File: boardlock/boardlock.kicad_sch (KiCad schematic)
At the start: 3 parts, among them U6 ESP32-S3-WROOM-1

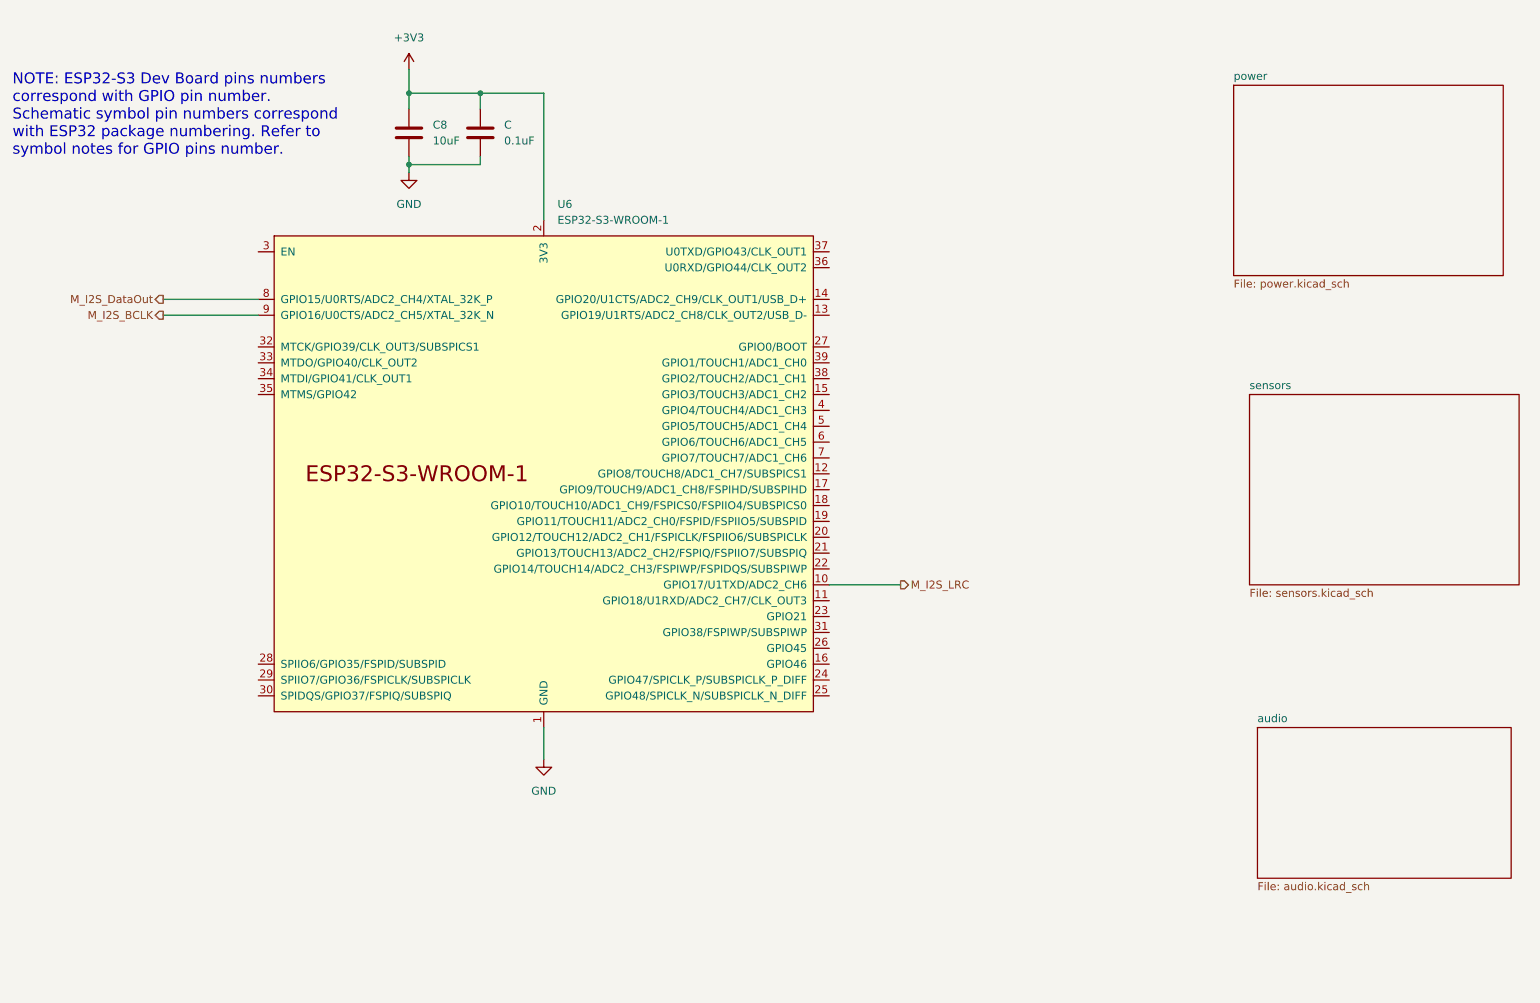
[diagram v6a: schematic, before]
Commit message: Added power library and fixed labels
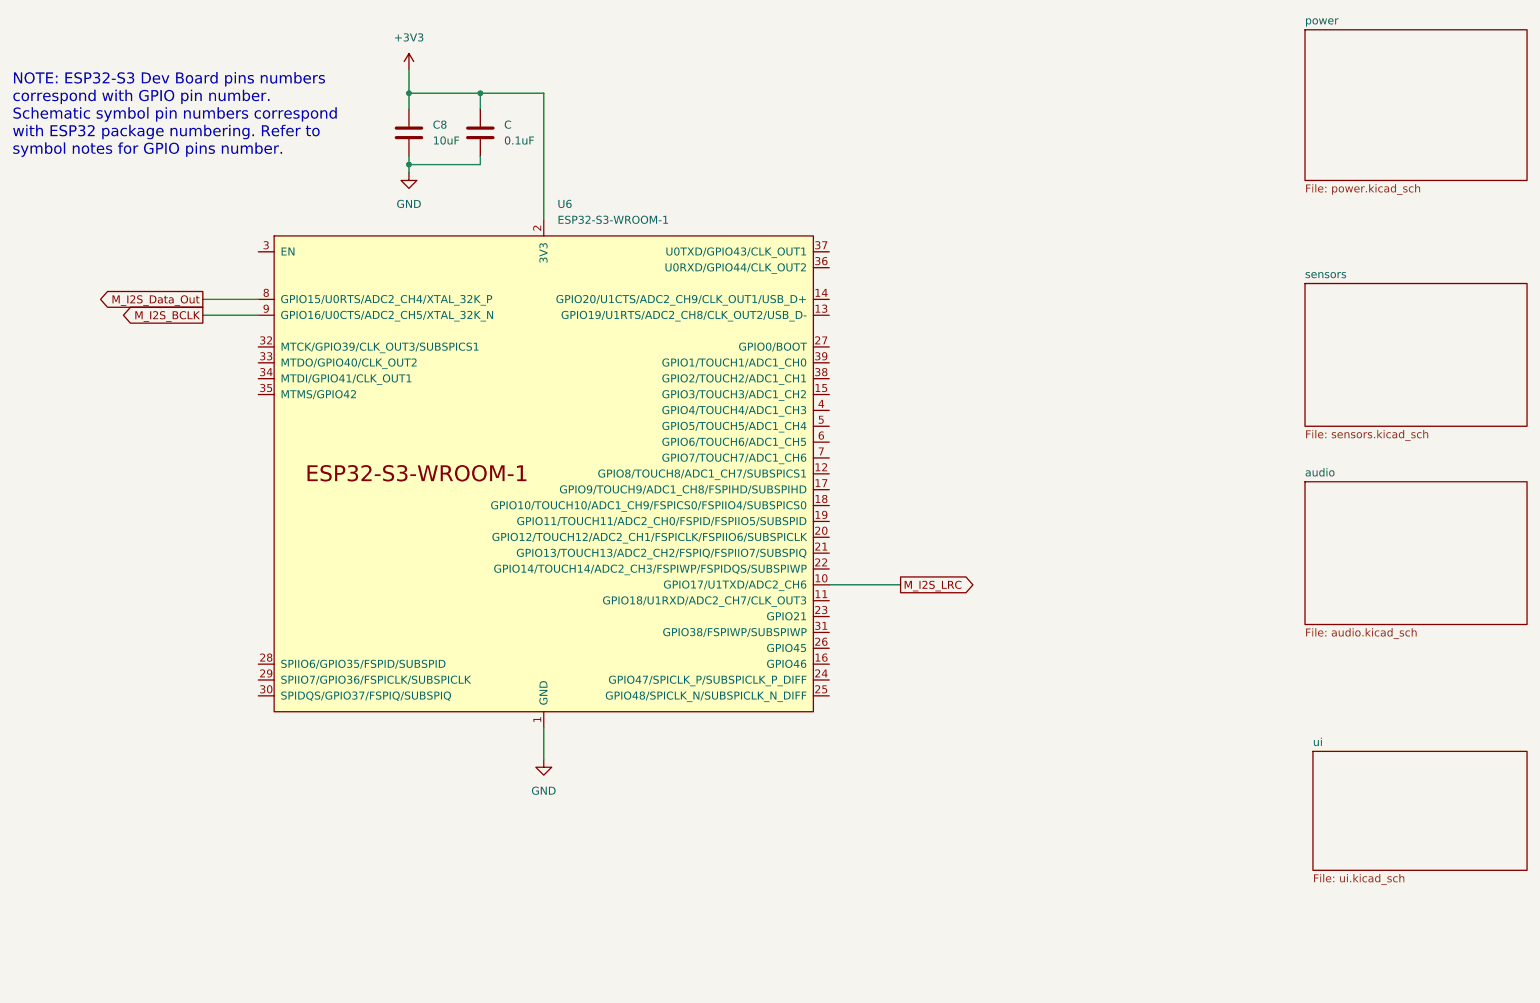
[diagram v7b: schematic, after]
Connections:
- net M_I2S_DataOut renamed M_I2S_Data_Out
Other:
- added sheet ui (ui.kicad_sch)
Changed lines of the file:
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@@
     (stroke (width 0) (type default))
   )
-  (wire (pts (xy 40.64 64.77) (xy 55.88 64.77))
+  (wire (pts (xy 46.99 64.77) (xy 55.88 64.77))
     (stroke (width 0) (type default))
   )
@@
     (stroke (width 0) (type default))
   )
-  (wire (pts (xy 40.64 62.23) (xy 55.88 62.23))
+  (wire (pts (xy 46.99 62.23) (xy 55.88 62.23))
     (stroke (width 0) (type default))
   )
@@
     (effects (font (size 1.75 1.75)) (justify left bottom))
   )
-  (hierarchical_label "M_I2S_DataOut" (shape output) (at 40.64 62.23 180) (fields_autoplaced)
+  (global_label "M_I2S_Data_Out" (shape output) (at 46.99 62.23 180) (fields_autoplaced)
     (effects (font (size 1.27 1.27)) (justify right))
-  )
-  (hierarchical_label "M_I2S_LRC" (shape output) (at 158.75 107.95 0) (fields_autoplaced)
+    (property "Intersheetrefs" "${INTERSHEET_REFS}" (at 29.1279 62.23 0)
+      (effects (font (size 1.27 1.27)) (justify right) hide)
+    )
+  )
+  (global_label "M_I2S_LRC" (shape output) (at 158.75 107.95 0) (fields_autoplaced)
     (effects (font (size 1.27 1.27)) (justify left))
-  )
-  (hierarchical_label "M_I2S_BCLK" (shape output) (at 40.64 64.77 180) (fields_autoplaced)
+    (property "Intersheetrefs" "${INTERSHEET_REFS}" (at 171.7137 107.95 0)
+      (effects (font (size 1.27 1.27)) (justify left) hide)
+    )
+  )
+  (global_label "M_I2S_BCLK" (shape output) (at 46.99 64.77 180) (fields_autoplaced)
     (effects (font (size 1.27 1.27)) (justify right))
+    (property "Intersheetrefs" "${INTERSHEET_REFS}" (at 32.7563 64.77 0)
+      (effects (font (size 1.27 1.27)) (justify right) hide)
+    )
   )
   (symbol (lib_id "power:GND") (at 80.01 41.91 0) (unit 1)
@@
     )
   )
-  (sheet (at 215.9 130.81) (size 40.64 24.13) (fields_autoplaced)
+  (sheet (at 223.52 91.44) (size 35.56 22.86) (fields_autoplaced)
     (stroke (width 0.1524) (type solid))
     (fill (color 0 0 0 0.0000))
-    (property "Sheetname" "audio" (at 215.9 130.0984 0)
+    (property "Sheetname" "audio" (at 223.52 90.7284 0)
       (effects (font (size 1.27 1.27)) (justify left bottom))
     )
-    (property "Sheetfile" "audio.kicad_sch" (at 215.9 155.5246 0)
+    (property "Sheetfile" "audio.kicad_sch" (at 223.52 114.8846 0)
       (effects (font (size 1.27 1.27)) (justify left top))
     )
@@
     )
   )
-  (sheet (at 212.09 27.94) (size 43.18 30.48) (fields_autoplaced)
+  (sheet (at 223.52 19.05) (size 35.56 24.13) (fields_autoplaced)
     (stroke (width 0.1524) (type solid))
     (fill (color 0 0 0 0.0000))
-    (property "Sheetname" "power" (at 212.09 27.2284 0)
+    (property "Sheetname" "power" (at 223.52 18.3384 0)
       (effects (font (size 1.27 1.27)) (justify left bottom))
     )
-    (property "Sheetfile" "power.kicad_sch" (at 212.09 59.0046 0)
+    (property "Sheetfile" "power.kicad_sch" (at 223.52 43.7646 0)
       (effects (font (size 1.27 1.27)) (justify left top))
     )
@@
     )
   )
-  (sheet (at 214.63 77.47) (size 43.18 30.48) (fields_autoplaced)
+  (sheet (at 223.52 59.69) (size 35.56 22.86) (fields_autoplaced)
     (stroke (width 0.1524) (type solid))
     (fill (color 0 0 0 0.0000))
-    (property "Sheetname" "sensors" (at 214.63 76.7584 0)
+    (property "Sheetname" "sensors" (at 223.52 58.9784 0)
       (effects (font (size 1.27 1.27)) (justify left bottom))
     )
-    (property "Sheetfile" "sensors.kicad_sch" (at 214.63 108.5346 0)
+    (property "Sheetfile" "sensors.kicad_sch" (at 223.52 83.1346 0)
       (effects (font (size 1.27 1.27)) (justify left top))
     )
@@
       )
     )
+  )
+  (sheet (at 224.79 134.62) (size 34.29 19.05) (fields_autoplaced)
+    (stroke (width 0.1524) (type solid))
+    (fill (color 0 0 0 0.0000))
+    (property "Sheetname" "ui" (at 224.79 133.9084 0)
+      (effects (font (size 1.27 1.27)) (justify left bottom))
+    )
+    (property "Sheetfile" "ui.kicad_sch" (at 224.79 154.2546 0)
+      (effects (font (size 1.27 1.27)) (justify left top))
+    )
+    (instances
+      (project "boardlock"
+        (path "/e1fc29ce-837e-4062-84d8-c7e423f9eab9" (page "5"))
+      )
+    )

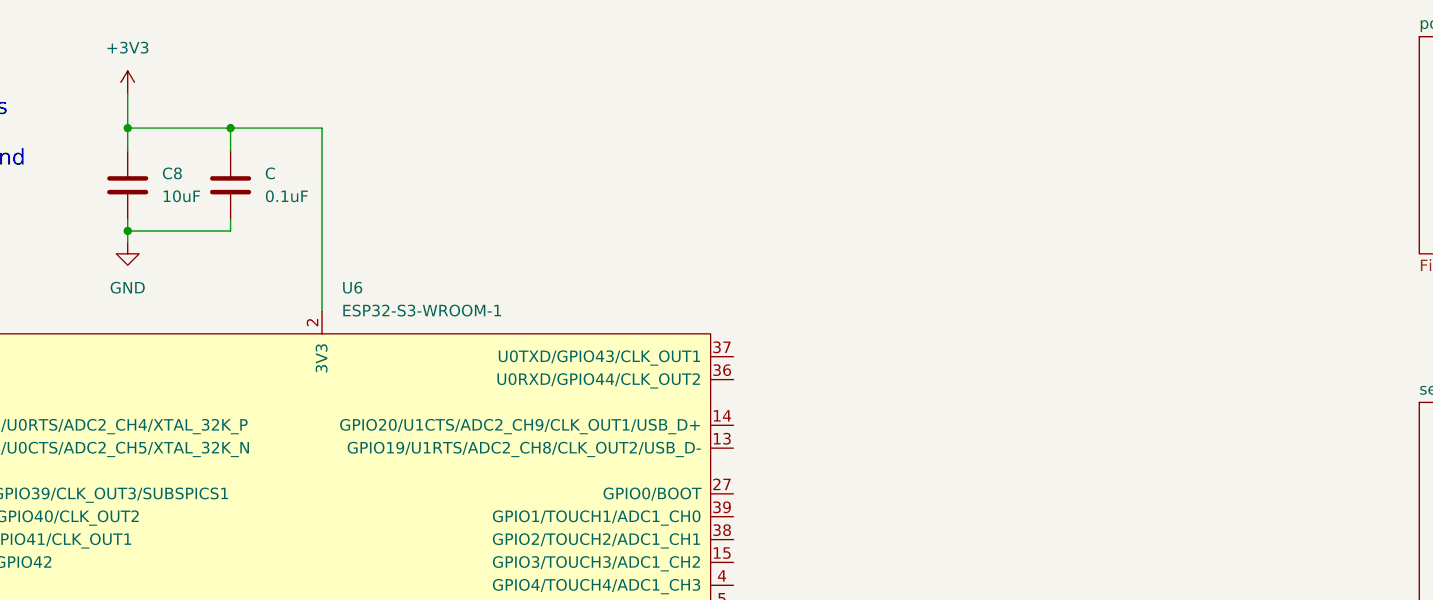
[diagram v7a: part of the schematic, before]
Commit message: added buck boost topology
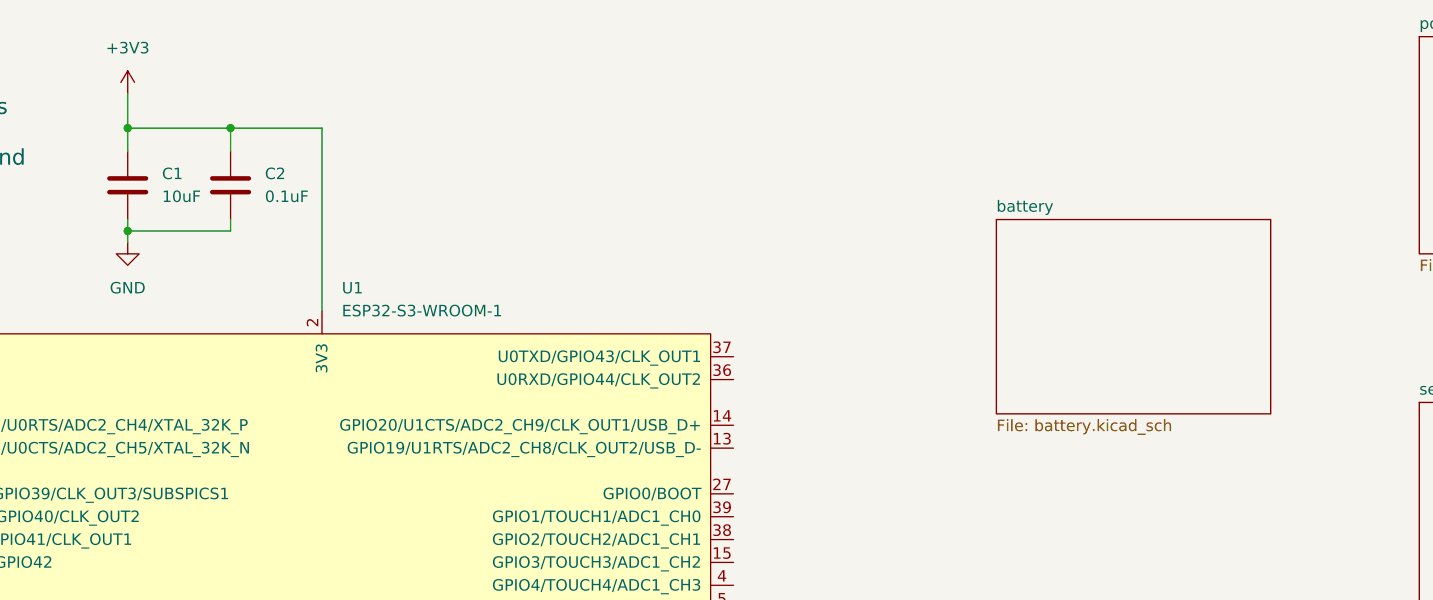
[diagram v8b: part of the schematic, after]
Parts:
- renumbered C8 to C1, C to C2, U6 to U1
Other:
- added sheet battery (battery.kicad_sch)
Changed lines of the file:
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@@
   (symbol (lib_id "power:GND") (at 80.01 41.91 0) (unit 1)
     (in_bom yes) (on_board yes) (dnp no) (fields_autoplaced)
-    (property "Reference" "#PWR021" (at 80.01 48.26 0)
+    (property "Reference" "#PWR02" (at 80.01 48.26 0)
       (effects (font (size 1.27 1.27)) hide)
     )
@@
       (project "boardlock"
         (path "/e1fc29ce-837e-4062-84d8-c7e423f9eab9"
-          (reference "#PWR021") (unit 1)
+          (reference "#PWR02") (unit 1)
         )
       )
@@
   (symbol (lib_id "PCM_Espressif:ESP32-S3-WROOM-1") (at 101.6 90.17 0) (unit 1)
     (in_bom yes) (on_board yes) (dnp no) (fields_autoplaced)
-    (property "Reference" "U6" (at 103.7941 46.99 0)
+    (property "Reference" "U1" (at 103.7941 46.99 0)
       (effects (font (size 1.27 1.27)) (justify left))
     )
@@
       (project "boardlock"
         (path "/e1fc29ce-837e-4062-84d8-c7e423f9eab9"
-          (reference "U6") (unit 1)
+          (reference "U1") (unit 1)
         )
       )
@@
   (symbol (lib_id "power:+3V3") (at 80.01 25.4 0) (unit 1)
     (in_bom yes) (on_board yes) (dnp no) (fields_autoplaced)
-    (property "Reference" "#PWR019" (at 80.01 29.21 0)
+    (property "Reference" "#PWR01" (at 80.01 29.21 0)
       (effects (font (size 1.27 1.27)) hide)
     )
@@
       (project "boardlock"
         (path "/e1fc29ce-837e-4062-84d8-c7e423f9eab9"
-          (reference "#PWR019") (unit 1)
+          (reference "#PWR01") (unit 1)
         )
       )
@@
   (symbol (lib_id "power:GND") (at 101.6 135.89 0) (unit 1)
     (in_bom yes) (on_board yes) (dnp no) (fields_autoplaced)
-    (property "Reference" "#PWR020" (at 101.6 142.24 0)
+    (property "Reference" "#PWR03" (at 101.6 142.24 0)
       (effects (font (size 1.27 1.27)) hide)
     )
@@
       (project "boardlock"
         (path "/e1fc29ce-837e-4062-84d8-c7e423f9eab9"
-          (reference "#PWR020") (unit 1)
+          (reference "#PWR03") (unit 1)
         )
       )
@@
   (symbol (lib_id "Device:C") (at 80.01 35.56 0) (unit 1)
     (in_bom yes) (on_board yes) (dnp no) (fields_autoplaced)
-    (property "Reference" "C8" (at 83.82 34.29 0)
+    (property "Reference" "C1" (at 83.82 34.29 0)
       (effects (font (size 1.27 1.27)) (justify left))
     )
@@
       (project "boardlock"
         (path "/e1fc29ce-837e-4062-84d8-c7e423f9eab9"
-          (reference "C8") (unit 1)
+          (reference "C1") (unit 1)
         )
       )
@@
   (symbol (lib_id "Device:C") (at 91.44 35.56 0) (unit 1)
     (in_bom yes) (on_board yes) (dnp no) (fields_autoplaced)
-    (property "Reference" "C" (at 95.25 34.29 0)
+    (property "Reference" "C2" (at 95.25 34.29 0)
       (effects (font (size 1.27 1.27)) (justify left))
     )
@@
       (project "boardlock"
         (path "/e1fc29ce-837e-4062-84d8-c7e423f9eab9"
-          (reference "C") (unit 1)
+          (reference "C2") (unit 1)
         )
       )
@@
       )
       (project "boardlock"
+        (path "/e1fc29ce-837e-4062-84d8-c7e423f9eab9" (page "5"))
+      )
+    )
+  )
+  (sheet (at 223.52 19.05) (size 35.56 24.13) (fields_autoplaced)
+    (stroke (width 0.1524) (type solid))
+    (fill (color 0 0 0 0.0000))
+    (property "Sheetname" "power" (at 223.52 18.3384 0)
+      (effects (font (size 1.27 1.27)) (justify left bottom))
+    )
+    (property "Sheetfile" "power.kicad_sch" (at 223.52 43.7646 0)
+      (effects (font (size 1.27 1.27)) (justify left top))
+    )
+    (instances
+      (project "boardlock"
+        (path "/48f24f42-fd64-4860-9f12-ca34cf195758" (page "3"))
+      )
+      (project "boardlock"
         (path "/e1fc29ce-837e-4062-84d8-c7e423f9eab9" (page "4"))
       )
     )
   )
-  (sheet (at 223.52 19.05) (size 35.56 24.13) (fields_autoplaced)
-    (stroke (width 0.1524) (type solid))
-    (fill (color 0 0 0 0.0000))
-    (property "Sheetname" "power" (at 223.52 18.3384 0)
-      (effects (font (size 1.27 1.27)) (justify left bottom))
-    )
-    (property "Sheetfile" "power.kicad_sch" (at 223.52 43.7646 0)
+  (sheet (at 176.53 39.37) (size 30.48 21.59) (fields_autoplaced)
+    (stroke (width 0.1524) (type solid))
+    (fill (color 0 0 0 0.0000))
+    (property "Sheetname" "battery" (at 176.53 38.6584 0)
+      (effects (font (size 1.27 1.27)) (justify left bottom))
+    )
+    (property "Sheetfile" "battery.kicad_sch" (at 176.53 61.5446 0)
+      (effects (font (size 1.27 1.27)) (justify left top))
+    )
+    (instances
+      (project "boardlock"
+        (path "/e1fc29ce-837e-4062-84d8-c7e423f9eab9" (page "3"))
+      )
+    )
+  )
+  (sheet (at 223.52 59.69) (size 35.56 22.86) (fields_autoplaced)
+    (stroke (width 0.1524) (type solid))
+    (fill (color 0 0 0 0.0000))
+    (property "Sheetname" "sensors" (at 223.52 58.9784 0)
+      (effects (font (size 1.27 1.27)) (justify left bottom))
+    )
+    (property "Sheetfile" "sensors.kicad_sch" (at 223.52 83.1346 0)
       (effects (font (size 1.27 1.27)) (justify left top))
     )
@@
       )
       (project "boardlock"
-        (path "/e1fc29ce-837e-4062-84d8-c7e423f9eab9" (page "3"))
-      )
-    )
-  )
-  (sheet (at 223.52 59.69) (size 35.56 22.86) (fields_autoplaced)
-    (stroke (width 0.1524) (type solid))
-    (fill (color 0 0 0 0.0000))
-    (property "Sheetname" "sensors" (at 223.52 58.9784 0)
-      (effects (font (size 1.27 1.27)) (justify left bottom))
-    )
-    (property "Sheetfile" "sensors.kicad_sch" (at 223.52 83.1346 0)
-      (effects (font (size 1.27 1.27)) (justify left top))
-    )
-    (instances
-      (project "boardlock"
-        (path "/48f24f42-fd64-4860-9f12-ca34cf195758" (page "3"))
-      )
-      (project "boardlock"
         (path "/e1fc29ce-837e-4062-84d8-c7e423f9eab9" (page "2"))
       )
@@
     (instances
       (project "boardlock"
-        (path "/e1fc29ce-837e-4062-84d8-c7e423f9eab9" (page "5"))
-      )
-    )
+        (path "/e1fc29ce-837e-4062-84d8-c7e423f9eab9" (page "6"))
+      )
+    )
